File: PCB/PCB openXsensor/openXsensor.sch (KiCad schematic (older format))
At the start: 18 parts, among them P1 Digital, P10 VFAS/COURANT, P11 GY-86, P12 NTC1, P13 NTC2, P14 ISP1, P15 ISP2, P16 4S, P17 ADS1115, P2 Analog, P3 ADC, P4 ADC, P5 GPS, P6 HUB/SPORT, P7 PPM, P8 FUEL, P9 RPM

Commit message: Move connector on sides.
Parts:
- R1: footprint R_1206 -> R_Axial_DIN0204_L3.6mm_D1.6mm_P7.62mm_Horizontal
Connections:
- net 1(Tx): now also P5.1 (Pin_1); no longer P5.3 (Pin_3)
- net 2: now also P7.2 (Pin_2); no longer P7.1 (Pin_1)
- net 4: now also P6.2 (Pin_2); no longer P6.1 (Pin_1)
- net 8: now also P9.3 (Pin_3); no longer P9.2 (Pin_2)
- net 9(**): now also P8.3 (Pin_3); no longer P8.2 (Pin_2)
- net GND: now also P6.1 (Pin_1), P7.1 (Pin_1), P8.2 (Pin_2), P9.2 (Pin_2); no longer P6.2 (Pin_2), P7.2 (Pin_2), P8.3 (Pin_3), P9.3 (Pin_3)
- net VCC: now also P5.3 (Pin_3); no longer P5.1 (Pin_1)
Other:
- note added: "Programmation (option)"
- note removed: "Programmation"
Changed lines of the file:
@@
 Sheet 1 1
 Title ""
-Date "2019-09-07"
+Date "2019-09-14"
 Rev ""
 Comp ""
@@
 F 0 "R1" V 4400 3450 50  0000 C CNN
 F 1 "10K" V 4450 3600 50  0000 C CNN
-F 2 "R_1206" V 4380 3600 50  0001 C CNN
+F 2 "R_Axial_DIN0204_L3.6mm_D1.6mm_P7.62mm_Horizontal" V 4380 3600 50  0001 C CNN
 F 3 "~" H 4450 3600 50  0001 C CNN
 	1    4450 3600
@@
 Wire Wire Line
 	4000 1150 2450 1150
-Wire Wire Line
-	3900 2800 3900 1250
-Wire Wire Line
-	3900 1250 2450 1250
 Wire Wire Line
 	3900 2800 4950 2800
@@
 P 2550 1350
 F 0 "#PWR0101" H 2550 1100 50  0001 C CNN
-F 1 "GND" H 2550 1200 50  0000 C CNN
+F 1 "GND" V 2550 1150 50  0000 C CNN
 F 2 "" H 2550 1350 50  0000 C CNN
 F 3 "" H 2550 1350 50  0000 C CNN
@@
 L power:GND #PWR0102
 U 1 1 5D74454D
-P 2550 1850
-F 0 "#PWR0102" H 2550 1600 50  0001 C CNN
-F 1 "GND" H 2550 1700 50  0000 C CNN
-F 2 "" H 2550 1850 50  0000 C CNN
-F 3 "" H 2550 1850 50  0000 C CNN
-	1    2550 1850
+P 2550 1750
+F 0 "#PWR0102" H 2550 1500 50  0001 C CNN
+F 1 "GND" H 2550 1600 50  0000 C CNN
+F 2 "" H 2550 1750 50  0000 C CNN
+F 3 "" H 2550 1750 50  0000 C CNN
+	1    2550 1750
 	0    -1   -1   0
 $EndComp
@@
 L power:GND #PWR0103
 U 1 1 5D744588
-P 2550 2300
-F 0 "#PWR0103" H 2550 2050 50  0001 C CNN
-F 1 "GND" H 2550 2150 50  0000 C CNN
-F 2 "" H 2550 2300 50  0000 C CNN
-F 3 "" H 2550 2300 50  0000 C CNN
-	1    2550 2300
-	0    -1   -1   0
-$EndComp
-Wire Wire Line
-	2550 2300 2450 2300
-Wire Wire Line
-	2550 1850 2450 1850
+P 2550 2200
+F 0 "#PWR0103" H 2550 1950 50  0001 C CNN
+F 1 "GND" H 2550 2050 50  0000 C CNN
+F 2 "" H 2550 2200 50  0000 C CNN
+F 3 "" H 2550 2200 50  0000 C CNN
+	1    2550 2200
+	0    -1   -1   0
+$EndComp
 $Comp
 L power:VCC #PWR0104
 U 1 1 5D746203
-P 2550 1050
-F 0 "#PWR0104" H 2550 900 50  0001 C CNN
-F 1 "VCC" H 2550 1200 50  0000 C CNN
-F 2 "" H 2550 1050 50  0000 C CNN
-F 3 "" H 2550 1050 50  0000 C CNN
-	1    2550 1050
+P 2550 1250
+F 0 "#PWR0104" H 2550 1100 50  0001 C CNN
+F 1 "VCC" V 2550 1450 50  0000 C CNN
+F 2 "" H 2550 1250 50  0000 C CNN
+F 3 "" H 2550 1250 50  0000 C CNN
+	1    2550 1250
 	0    1    1    0
 $EndComp
 Wire Wire Line
-	2450 1050 2550 1050
-Wire Wire Line
-	3800 3400 3800 1750
-Wire Wire Line
-	3800 1750 2450 1750
+	3800 3400 3800 1850
 Wire Wire Line
 	3800 3400 4950 3400
 Wire Wire Line
-	3700 3200 3700 2200
-Wire Wire Line
-	3700 2200 2450 2200
+	3700 3200 3700 2300
 Wire Wire Line
 	3700 3200 4950 3200
@@
 Wire Wire Line
 	3500 3900 4950 3900
-Wire Wire Line
-	3500 2750 2450 2750
-Wire Wire Line
-	3600 3200 2450 3200
-Wire Wire Line
-	3600 3200 3600 3800
-Wire Wire Line
-	3500 2750 3500 3900
 $Comp
 L power:GND #PWR0105
 U 1 1 5D74C7E6
-P 2550 3300
-F 0 "#PWR0105" H 2550 3050 50  0001 C CNN
-F 1 "GND" H 2550 3150 50  0000 C CNN
-F 2 "" H 2550 3300 50  0000 C CNN
-F 3 "" H 2550 3300 50  0000 C CNN
-	1    2550 3300
+P 2550 3200
+F 0 "#PWR0105" H 2550 2950 50  0001 C CNN
+F 1 "GND" V 2550 3000 50  0000 C CNN
+F 2 "" H 2550 3200 50  0000 C CNN
+F 3 "" H 2550 3200 50  0000 C CNN
+	1    2550 3200
 	0    -1   -1   0
 $EndComp
@@
 L power:GND #PWR0106
 U 1 1 5D74C821
-P 2550 2850
-F 0 "#PWR0106" H 2550 2600 50  0001 C CNN
-F 1 "GND" H 2550 2700 50  0000 C CNN
-F 2 "" H 2550 2850 50  0000 C CNN
-F 3 "" H 2550 2850 50  0000 C CNN
-	1    2550 2850
-	0    -1   -1   0
-$EndComp
-Wire Wire Line
-	2550 3300 2450 3300
-Wire Wire Line
-	2550 2850 2450 2850
+P 2550 2750
+F 0 "#PWR0106" H 2550 2500 50  0001 C CNN
+F 1 "GND" V 2550 2550 50  0000 C CNN
+F 2 "" H 2550 2750 50  0000 C CNN
+F 3 "" H 2550 2750 50  0000 C CNN
+	1    2550 2750
+	0    -1   -1   0
+$EndComp
 $Comp
 L power:VCC #PWR0107
@@
 P 2550 3100
 F 0 "#PWR0107" H 2550 2950 50  0001 C CNN
-F 1 "VCC" H 2550 3250 50  0000 C CNN
+F 1 "VCC" V 2550 3300 50  0000 C CNN
 F 2 "" H 2550 3100 50  0000 C CNN
 F 3 "" H 2550 3100 50  0000 C CNN
@@
 P 2550 2650
 F 0 "#PWR0108" H 2550 2500 50  0001 C CNN
-F 1 "VCC" H 2550 2800 50  0000 C CNN
+F 1 "VCC" V 2550 2850 50  0000 C CNN
 F 2 "" H 2550 2650 50  0000 C CNN
 F 3 "" H 2550 2650 50  0000 C CNN
@@
 	7500 2750 7000 2750
 Text Notes 6950 2700 0    50   ~ 0
-Programmation
+Programmation (option)
 Text Notes 5250 4700 1    50   ~ 0
 SDA
@@
 $EndComp
 $Comp
-L power:VCC #PWR?
+L power:VCC #PWR0116
 U 1 1 5D77DD14
 P 2550 6500
-F 0 "#PWR?" H 2550 6350 50  0001 C CNN
+F 0 "#PWR0116" H 2550 6350 50  0001 C CNN
 F 1 "VCC" V 2550 6700 50  0000 C CNN
 F 2 "" H 2550 6500 50  0000 C CNN
@@
 $EndComp
 $Comp
-L power:GND #PWR?
+L power:GND #PWR0117
 U 1 1 5D77DD1A
 P 2550 6600
-F 0 "#PWR?" H 2550 6350 50  0001 C CNN
+F 0 "#PWR0117" H 2550 6350 50  0001 C CNN
 F 1 "GND" V 2550 6400 50  0000 C CNN
 F 2 "" H 2550 6600 50  0000 C CNN
@@
 Text Label 2700 6800 0    50   ~ 0
 A4
+Wire Wire Line
+	2450 2300 3700 2300
+Wire Wire Line
+	2450 1850 3800 1850
+Wire Wire Line
+	2450 1750 2550 1750
+Wire Wire Line
+	2450 2200 2550 2200
+Wire Wire Line
+	2550 2750 2450 2750
+Wire Wire Line
+	2450 2850 3500 2850
+Wire Wire Line
+	3500 2850 3500 3900
+Wire Wire Line
+	2450 3300 3600 3300
+Wire Wire Line
+	3600 3300 3600 3800
+Wire Wire Line
+	2450 3200 2550 3200
+Wire Wire Line
+	2550 1250 2450 1250
+Wire Wire Line
+	3900 1050 2450 1050
+Wire Wire Line
+	3900 1050 3900 2800
 $EndSCHEMATC

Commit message: Update oXs pcb proto
Add protection resistors for 4s ans sport/hub connectors.
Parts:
- removed P15: ISP2, Pin_Header_Straight_1x03_Pitch2.54mm, symbol Connector_Generic:Conn_01x03
- added P18: ADS_IN, Pin_Header_Straight_1x04_Pitch2.54mm, symbol Connector_Generic:Conn_01x04
- added P4-2: ADC, Socket_Arduino_Pro_Mini:Socket_Strip_Arduino_1x02, symbol Connector_Generic:Conn_01x02
- added R10: 220, R_1206, symbol Device:R
- added R2, R3, R4, R5: 20K, R_1206, symbol Device:R
- added R6, R7, R8, R9: 51K, R_1206, symbol Device:R
- P14: value ISP1 -> ALIM
- R1: footprint R_Axial_DIN0204_L3.6mm_D1.6mm_P7.62mm_Horizontal -> R_1206
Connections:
- net A0: now also R2.1, R6.2; no longer P10.3 (Pin_3)
- net A1: now also R3.1, R7.2; no longer P10.4 (Pin_4)
- net A2: now also R4.1, R8.2; no longer P16.1 (Pin_1)
- net A3: now also R5.1, R9.2; no longer P16.2 (Pin_2)
- net A6: now also P10.4 (Pin_4), P4-2.2 (Pin_2); no longer P16.3 (Pin_3)
- net A7: now also P10.3 (Pin_3), P4-2.1 (Pin_1); no longer P16.4 (Pin_4)
- net GND: now also P14.3 (Pin_3), R10.2, R2.2, R3.2, R4.2, R5.2; no longer P14.1 (Pin_1), P16.5 (Pin_5), P6.1 (Pin_1)
- net RAW: now also P14.1 (Pin_1)
- net VCC: now also P14.2 (Pin_2); no longer P14.3 (Pin_3)
- net NTC1: now reaches P12.1 (Pin_1)
- net NTC2: now reaches P13.1 (Pin_1)
- net at P17.10 (Pin_10): now also P18.4 (Pin_4)
- net at P17.7 (Pin_7): now also P18.1 (Pin_1)
- net at P17.8 (Pin_8): now also P18.2 (Pin_2)
- net at P17.9 (Pin_9): now also P18.3 (Pin_3)
- net Reset: no longer names the net of P2.3 (Pin_3)
- net Reset: no longer P14.2 (Pin_2)
- new net: P6.1 (Pin_1), R10.1
- new net: P16.1 (Pin_1), R6.1
- new net: P16.2 (Pin_2), R7.1
- new net: P16.3 (Pin_3), R8.1
- new net: P16.4 (Pin_4), R9.1
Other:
- note added: "RESET"
- note removed: "Programmation (option)"

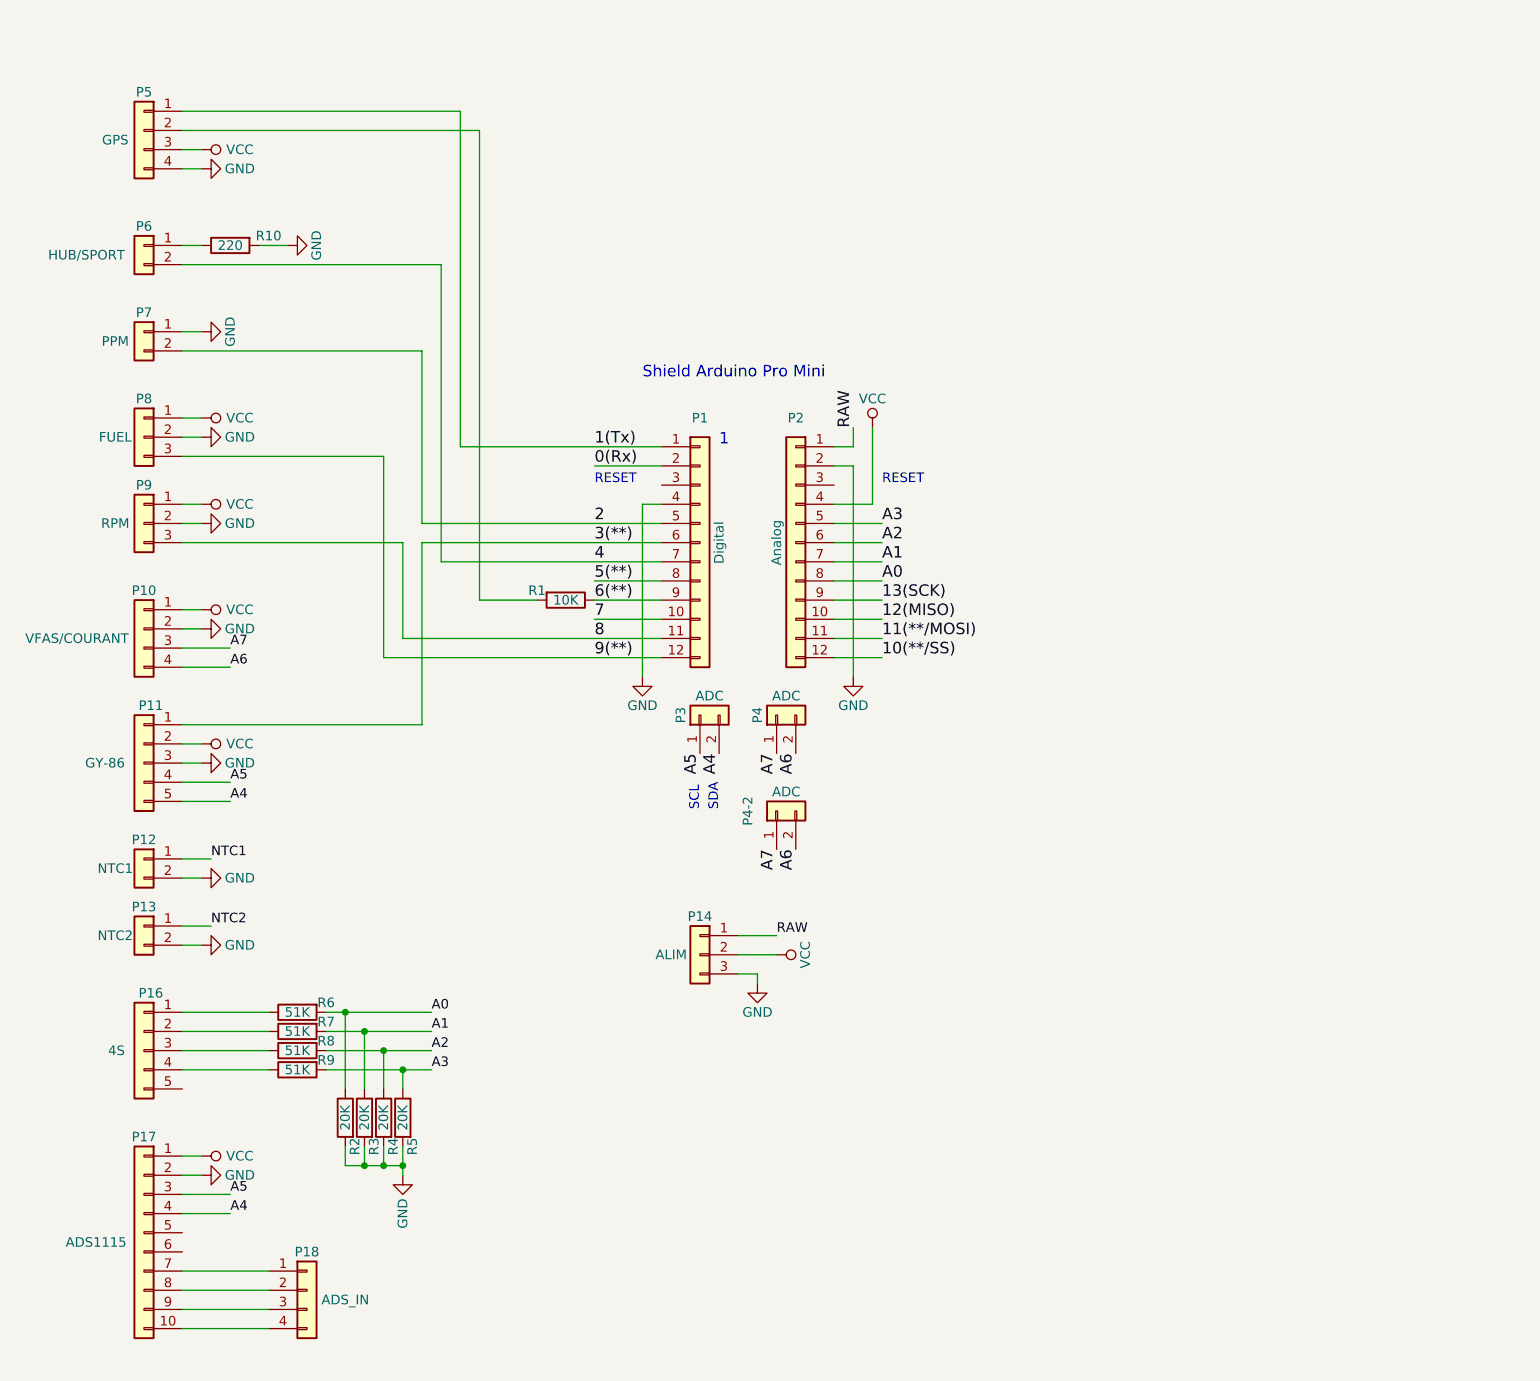
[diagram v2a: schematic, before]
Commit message: Update oXs pcb
Add resistors protection on Vfas et current
Add 5v pin on Sport connector
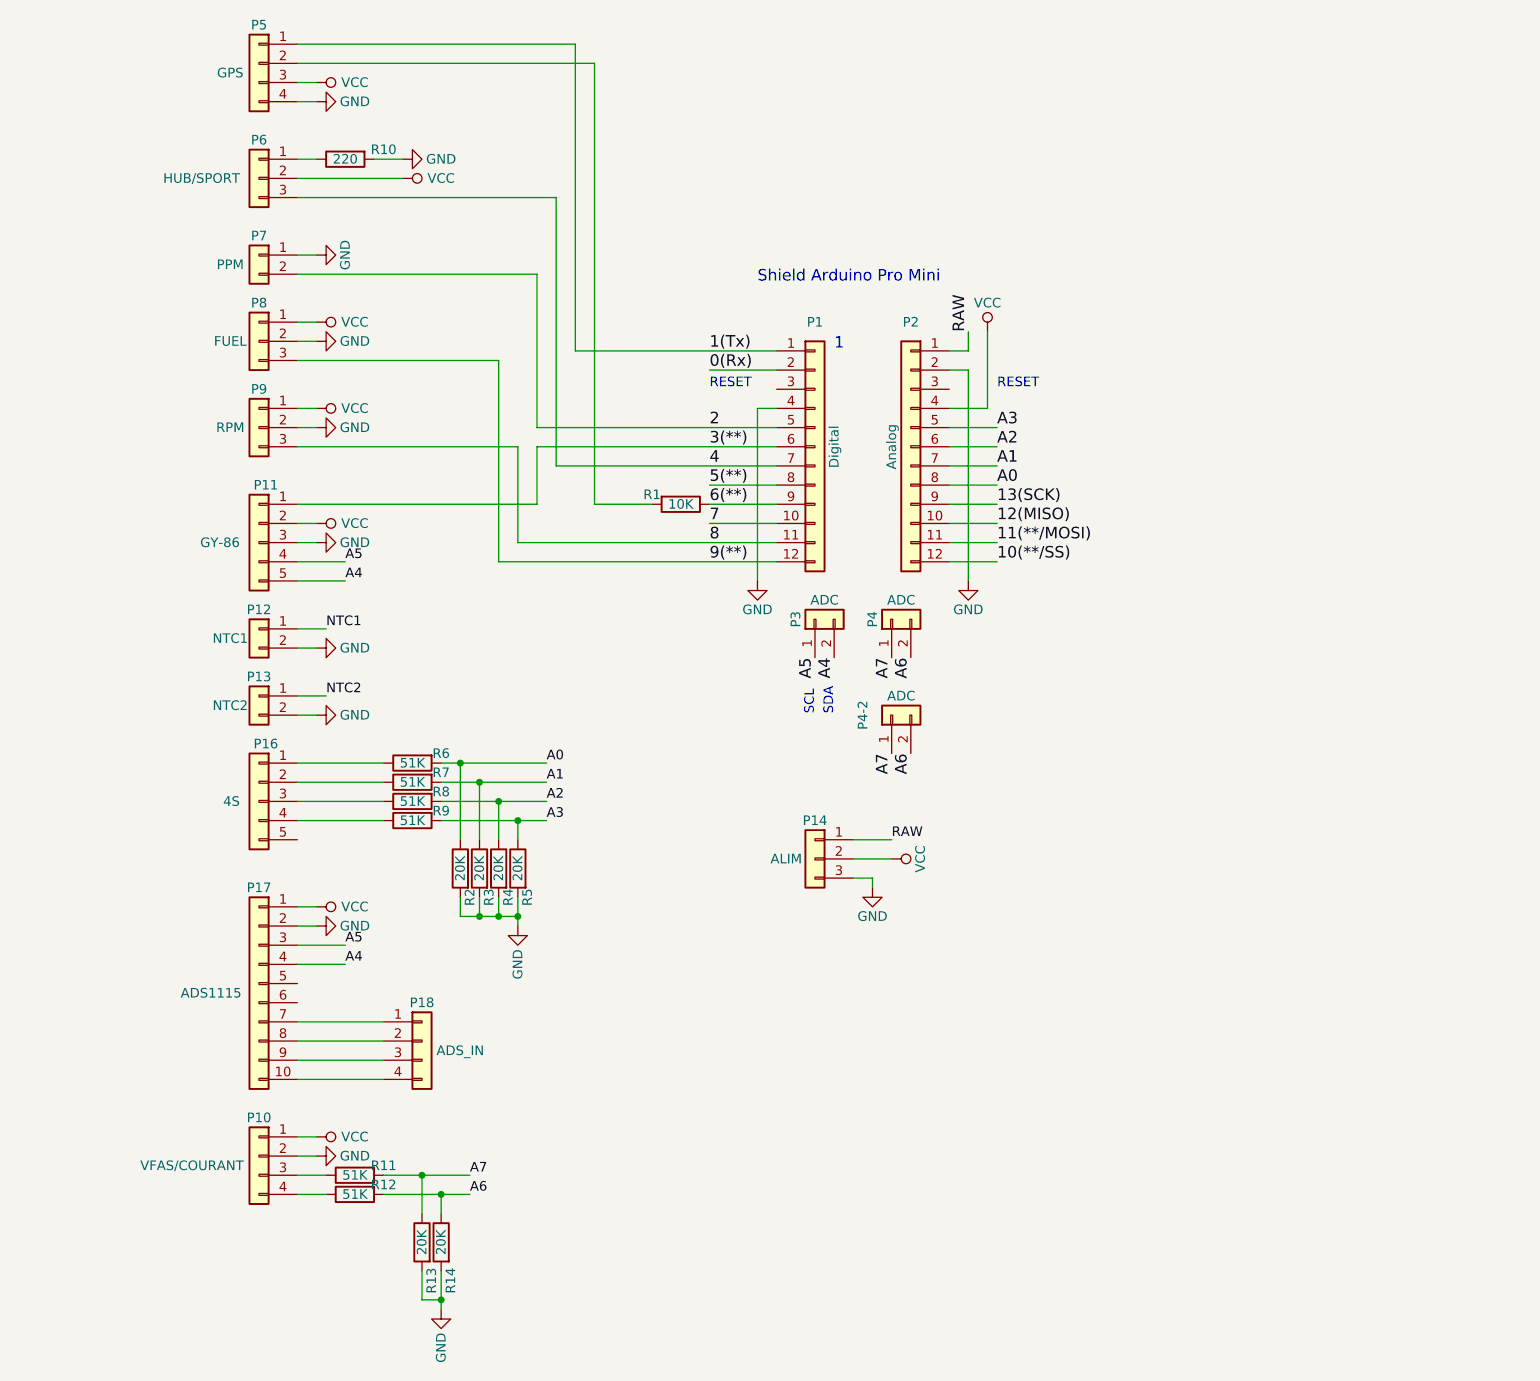
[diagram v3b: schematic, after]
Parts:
- removed P6: HUB/SPORT, Pin_Header_Straight_1x02_Pitch2.54mm, symbol Connector_Generic:Conn_01x02
- added P6: HUB/SPORT, Pin_Header_Straight_1x03_Pitch2.54mm, symbol Connector_Generic:Conn_01x03
- added R11, R12: 51K, R_1206, symbol Device:R
- added R13, R14: 20K, R_1206, symbol Device:R
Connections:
- net 4: now also P6.3 (Pin_3)
- net A6: now also R12.2, R14.1; no longer P10.4 (Pin_4)
- net A7: now also R11.2, R13.1; no longer P10.3 (Pin_3)
- net GND: now also R13.2, R14.2
- net VCC: now also P6.2 (Pin_2)
- net at R10.1: now also P6.1 (Pin_1)
- new net: P10.3 (Pin_3), R11.1
- new net: P10.4 (Pin_4), R12.1
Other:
- moved on the sheet: P1, P10, P11, P12, P13, P14, P16, P17, P18, P2, P3, P4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
